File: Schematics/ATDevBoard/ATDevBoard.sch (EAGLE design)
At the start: 40 parts, among them U1 TINY85-DIP

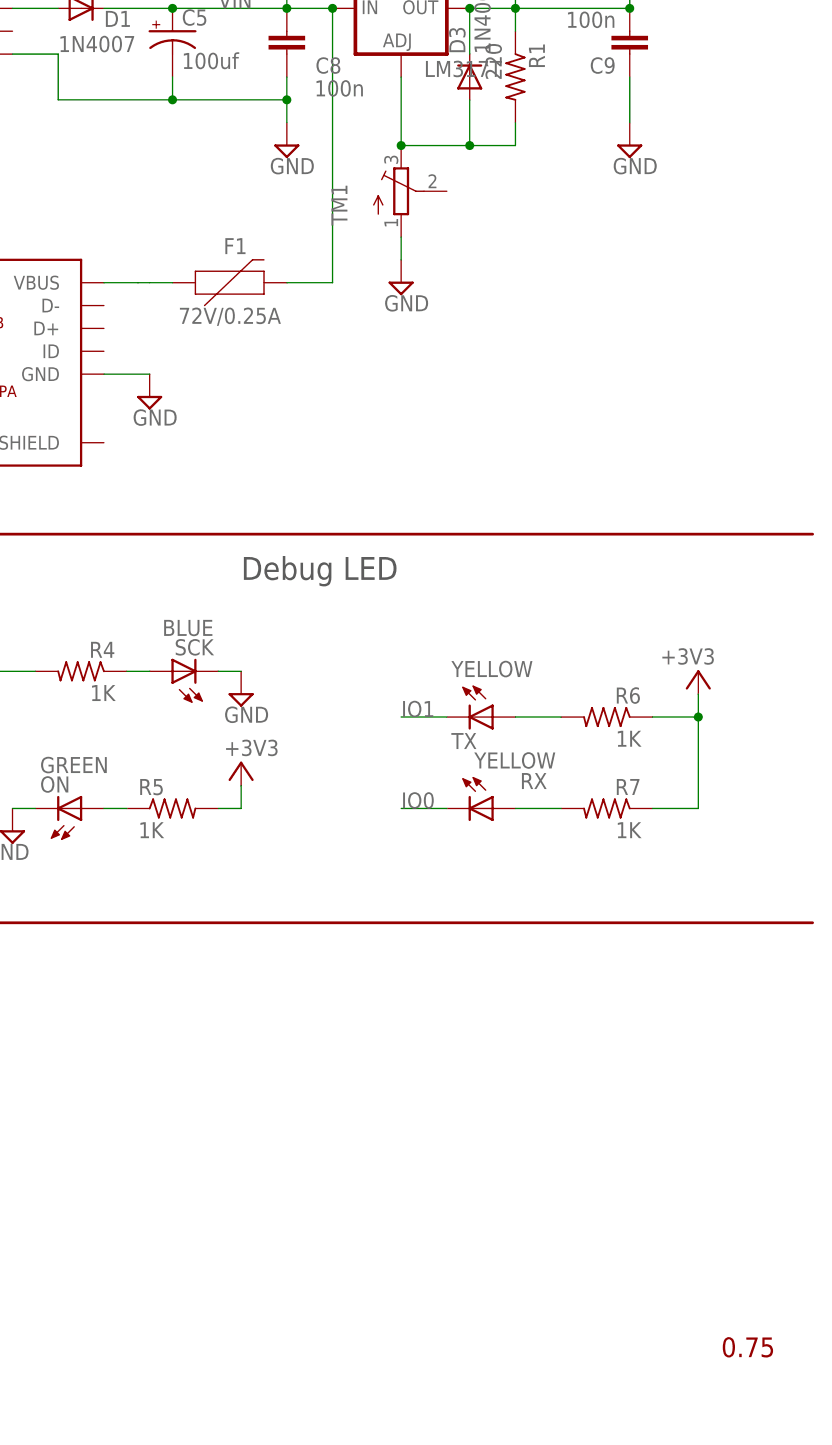
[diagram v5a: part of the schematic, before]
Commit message: Fixed package for trimmer
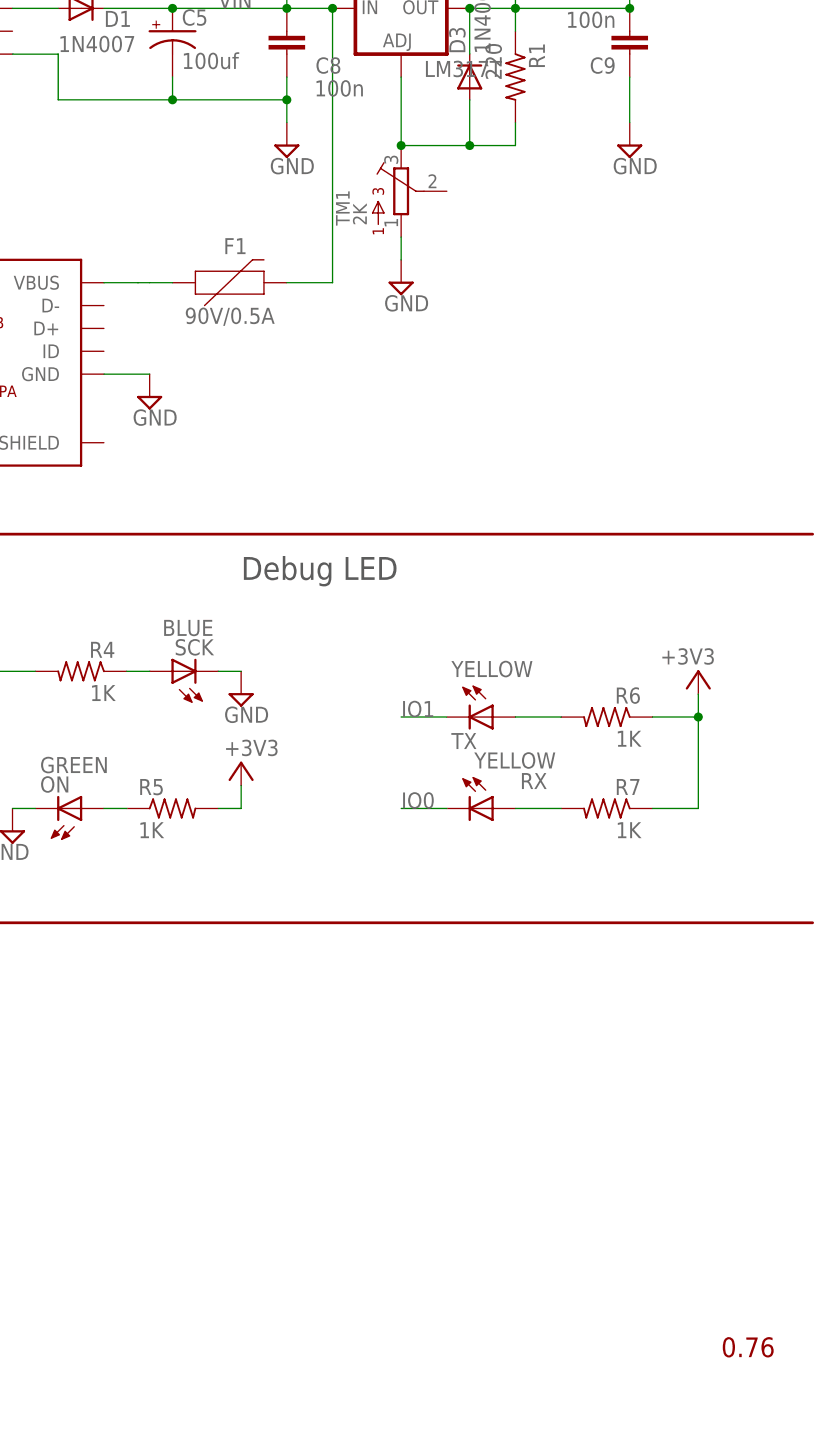
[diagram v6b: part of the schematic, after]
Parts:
- F1: value 72V/0.25A -> 90V/0.5A
- TM1: value (none) -> 2K; device adafruit:TRIMPOT3386 -> bourns:3362R
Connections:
- net GND: now also TM1.1; no longer TM1.A
- net N$1: now also TM1.3; no longer TM1.E
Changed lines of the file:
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@@
 <schematic xreflabel="%F%N/%S" xrefpart="/%S.%C%R">
 <attributes>
-<attribute name="VERSION" value="0.75"/>
+<attribute name="VERSION" value="0.76"/>
 </attributes>
 <variantdefs>
@@
 <clearance class="0" value="0.254"/>
 </class>
-<class number="1" name="power" width="0.6096" drill="0.6096">
+<class number="1" name="power" width="0.6096" drill="0.508">
 <clearance class="1" value="0.254"/>
 </class>
-<class number="2" name="gnd" width="0.3048" drill="0.5588">
+<class number="2" name="gnd" width="0.3048" drill="0.508">
 <clearance class="2" value="0.254"/>
 </class>
-<class number="3" name="aref" width="0.4064" drill="0.6096">
+<class number="3" name="aref" width="0.4064" drill="0.508">
 <clearance class="3" value="0.254"/>
 </class>
@@
 <part name="R7" library="rcl" deviceset="R-US_" device="0207/10" value="1K"/>
 <part name="D2" library="adafruit" deviceset="DIODE" device="SOD-323F" value="1N4148"/>
-<part name="F1" library="SparkFun-Fuses" deviceset="PPTC" device="_PTH" value="72V/0.25A"/>
-<part name="TM1" library="adafruit" deviceset="TRIMPOT" device="3386"/>
+<part name="F1" library="SparkFun-Fuses" deviceset="PPTC" device="_PTH" value="90V/0.5A"/>
+<part name="TM1" library="bourns" deviceset="3362" device="R" value="2K"/>
 <part name="SUPPLY2" library="supply2" deviceset="GND" device=""/>
 <part name="USB1" library="Seeed-Connector" deviceset="MICRO-USB-SMD(ZX62-B-5PA)" device="" value="ZX62-B-5PA"/>
@@
 <pinref part="SUPPLY1" gate="GND" pin="GND"/>
 <wire x1="241.3" y1="137.16" x2="241.3" y2="134.62" width="0.1524" layer="91"/>
-<pinref part="TM1" gate="G$1" pin="A"/>
+<pinref part="TM1" gate="G$1" pin="1"/>
 </segment>
 <segment>
@@
 <wire x1="248.92" y1="152.4" x2="248.92" y2="147.32" width="0.1524" layer="91"/>
 <junction x="248.92" y="147.32"/>
-<pinref part="TM1" gate="G$1" pin="E"/>
+<pinref part="TM1" gate="G$1" pin="3"/>
 <junction x="241.3" y="147.32"/>
 </segment>

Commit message: Replaced Dc plug with component in CuSTOM_GB library
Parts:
- JPOWER: device con-jack-plated-slots:JACK-PLUG0 -> CuSTOM_GB:JACK-PLUG0
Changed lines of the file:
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@@
 <part name="SUPPLY55" library="supply1" deviceset="+3V3" device=""/>
 <part name="SUPPLY1" library="supply2" deviceset="GND" device=""/>
-<part name="JPOWER" library="con-jack-plated-slots" deviceset="JACK-PLUG" device="0"/>
+<part name="JPOWER" library="CuSTOM_GB" deviceset="JACK-PLUG" device="0"/>
 <part name="D1" library="diode" deviceset="1N4004" device="" value="1N4007"/>
 <part name="RX" library="led" deviceset="LED" device="CHIPLED_1206" value="YELLOW"/>

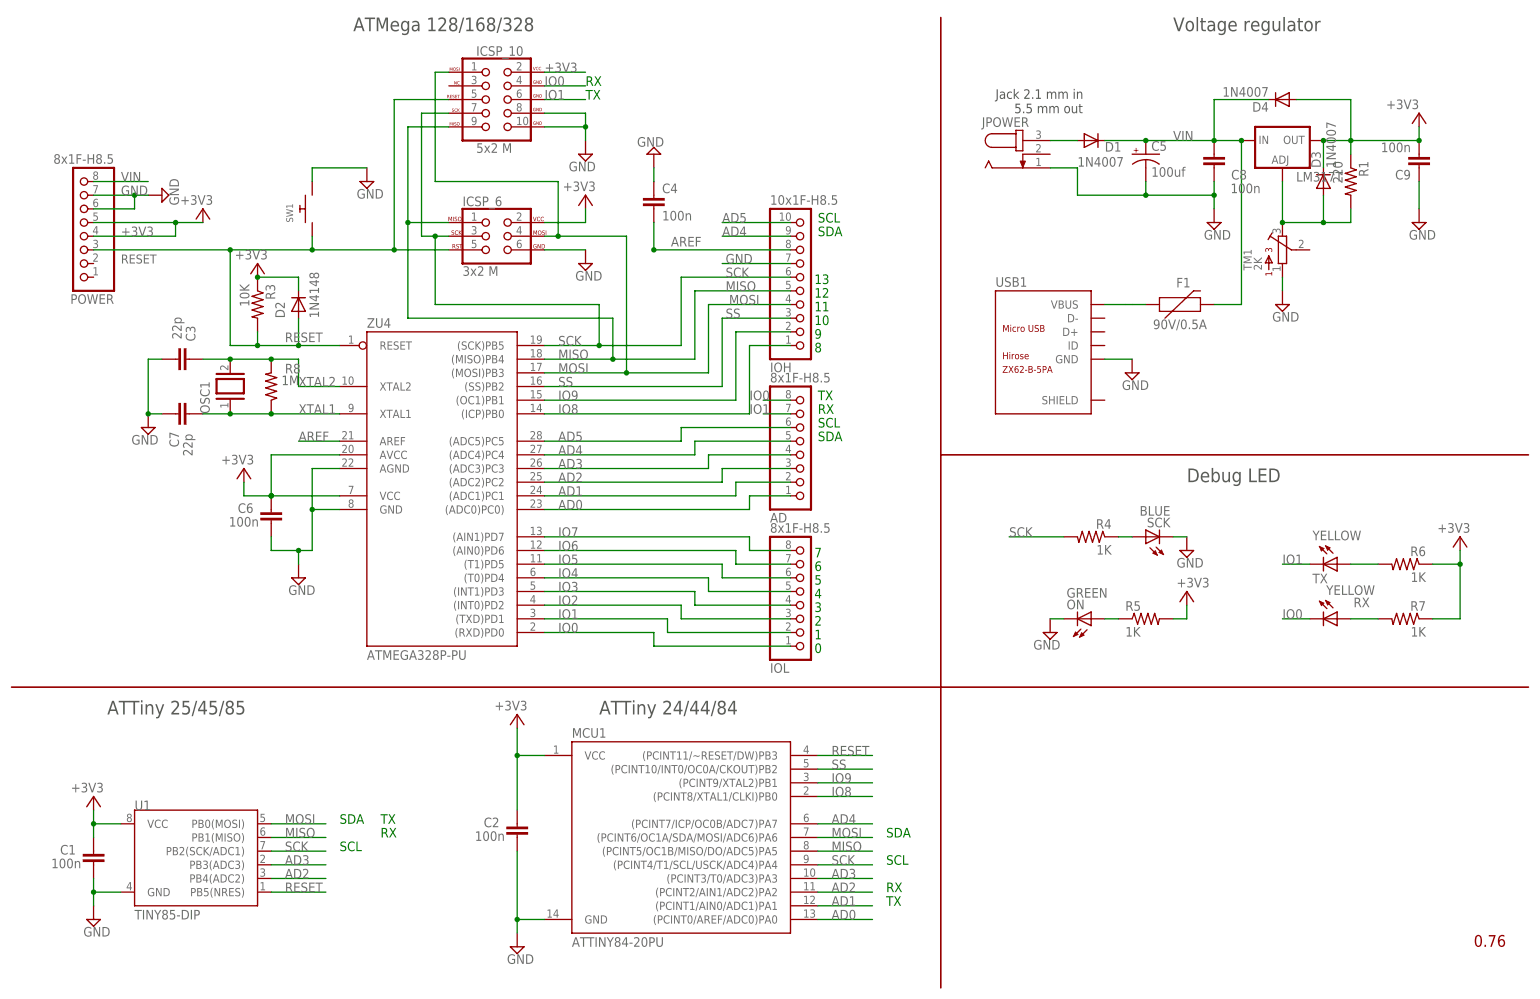
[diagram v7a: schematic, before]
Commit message: Changed size of power header to 5, added label for all signals in/out
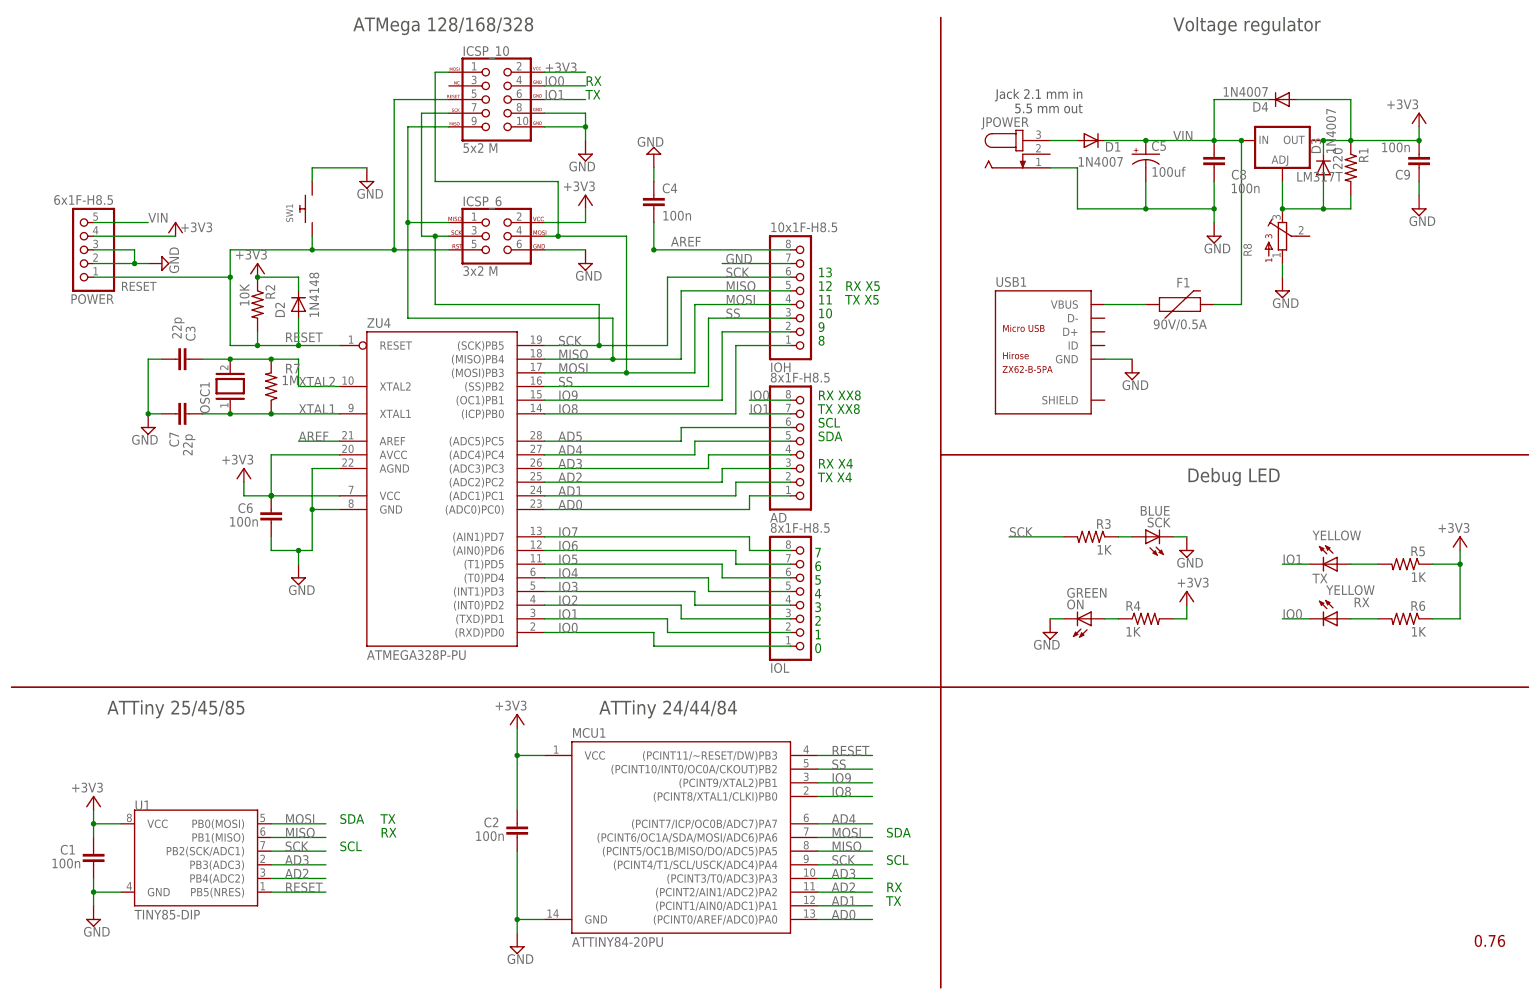
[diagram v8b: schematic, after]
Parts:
- removed TM1: 2K, bourns:3362R
- added R2: 10K, rcl:R-US_0309/12
- IOH: device pinhead:PINHD-1X10 -> pinhead:PINHD-1X8
- POWER: value 8x1F-H8.5 -> 6x1F-H8.5; device SmartPrj:PINHD-1X8 -> pinhead:PINHD-1X5
- R3: value 10K -> 1K; device rcl:R-US_0309/12 -> rcl:R-US_0207/10
- R7: value 1K -> 1M
- R8: value 1M -> (none); device rcl:R-US_0207/10 -> bourns:3362R
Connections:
- net +3V3: now also R2.1, R4.2, R5.1; no longer POWER.5, R3.1, R5.2, R7.1
- net AD4: no longer IOH.9
- net AD5: no longer IOH.10
- net GND: now also POWER.2, POWER.3, R8.1; no longer POWER.6, POWER.7, TM1.1
- net N$1: now also R8.3; no longer TM1.3
- net N$3: now also R4.1; no longer R5.1
- net N$35: now also R6.2; no longer R7.2
- net N$36: now also R5.2; no longer R6.2
- net N$4: now also R3.1; no longer R4.1
- net RESET: now also POWER.1, R2.2; no longer POWER.3, R3.2
- net SCK: now also R3.2; no longer R4.2
- net VIN: now also POWER.5; no longer POWER.8
- net XTAL1: now also R7.1; no longer R8.1
- net XTAL2: now also R7.2; no longer R8.2
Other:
- note added: "RX X4"
- note added: "RX X5"
- note added: "RX XX8"
- note added: "TX X4"
- note added: "TX X5"
- note added: "TX XX8"
- moved on the sheet: D3, R1, R3, R4, R5, R6, R7
